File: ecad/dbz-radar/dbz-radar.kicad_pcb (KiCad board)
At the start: 4 copper layers, 125.2 x 122.2 mm, 139 parts, among them J1 B2B-PH-SM4-TB, J2 USB4220-03-0880-C, J3 XF2M-4015-1A, J4 533980271, J5 Conn_01x12_Pin, Q1 Q_PMOS, SW1 SKRPACE010, SW2 SKRPACE010, SW3 1-825027-7, U1 USBLC6-2SC6, U2 TPS61169, U3 MCP738311/2, U4 MAX17048/9, U5 AP2112K-3.3, U6 PCA9554, U7 MAX98357A, U8 ESP32-S3-WROOM-1

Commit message: add part numbers to all components
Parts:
- C5: footprint Capacitor_SMD:C_0805_2012Metric_Pad1.18x1.45mm_HandSolder -> Capacitor_SMD:C_1206_3216Metric_Pad1.33x1.80mm_HandSolder
- J5: value Conn_01x12_Pin -> DNI
- moved C5 0.60 mm to (116.4, 69.3)

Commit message: output fabrication files
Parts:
- R6: value 8.2 -> 10
- U8: value ESP32-S3-WROOM-1 -> ESP32-S3-WROOM-1-N16R8

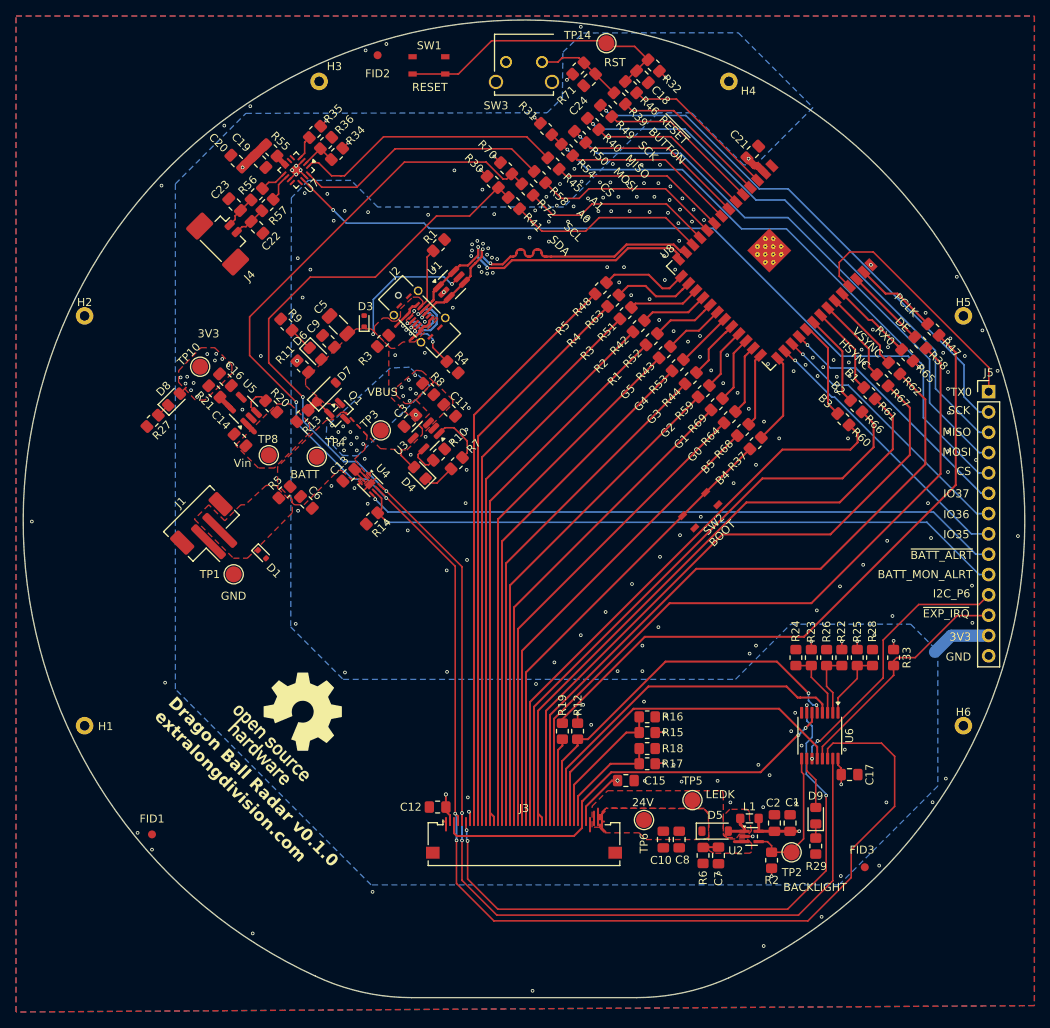
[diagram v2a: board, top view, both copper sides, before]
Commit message: flip polarity of battery connector, change to thinner stack up
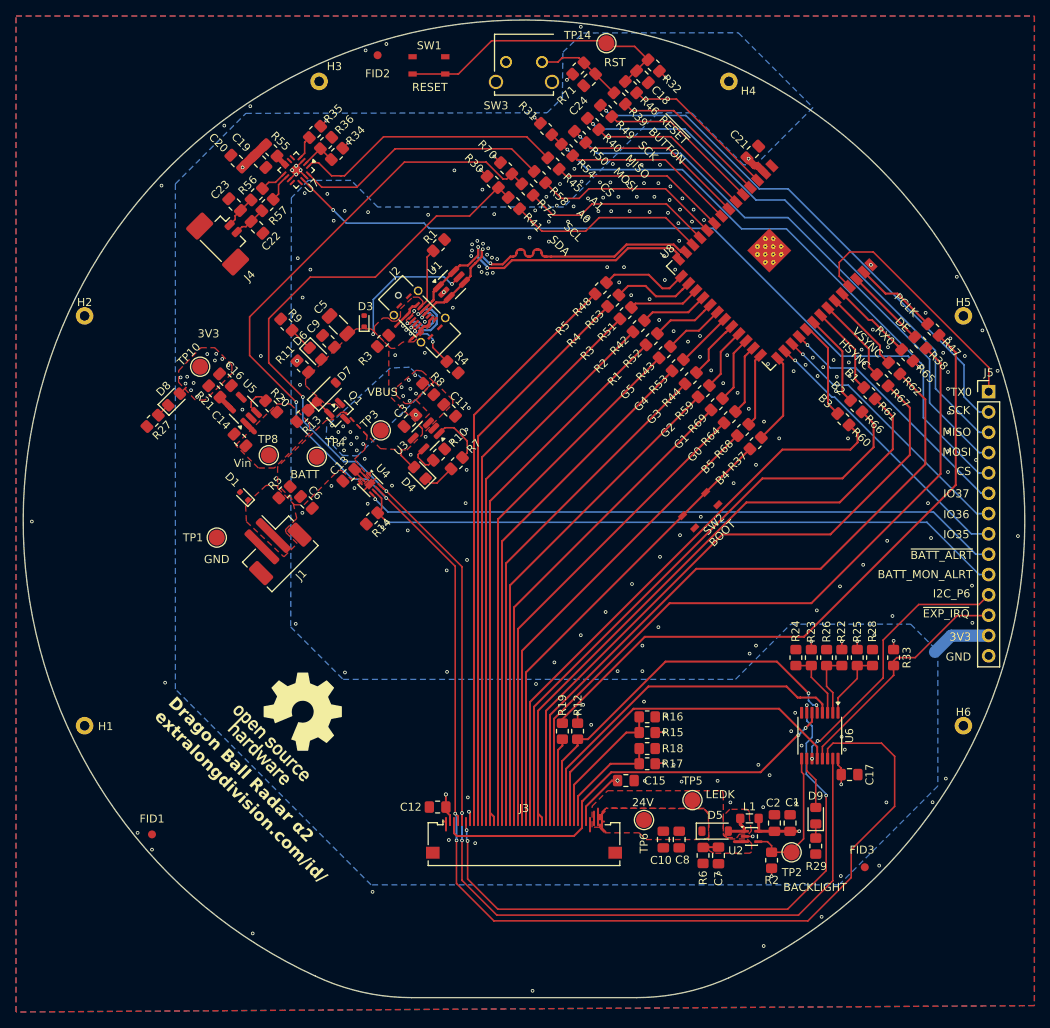
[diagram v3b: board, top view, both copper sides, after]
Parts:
- C21: value 100uF -> 100nF
- moved D1 7.63 mm to (104.6, 90.7), turned to 135 degrees
- moved J1 7.51 mm to (107.9, 96.7), turned to -135 degrees
- moved TP1 5.05 mm to (101.2, 95.9)
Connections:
- J1 pad 1: GND -> /BATT_CONN
- J1 pad 2: /BATT_CONN -> GND
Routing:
- net GND: vias 220 -> 227
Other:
- board text added: "Dragon Ball Radar α2 extralongdivision.com/id/"
- board text removed: "Dragon Ball Radar v0.1.0 extralongdivision.com"

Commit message: make production files for V1.2
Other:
- board text added: "Dragon Ball Radar V1.1 extralongdivision.com/id/"
- board text removed: "Dragon Ball Radar α2 extralongdivision.com/id/"
